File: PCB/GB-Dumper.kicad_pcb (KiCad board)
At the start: 2 copper layers, 89.5 x 72 mm, 27 parts, among them J1 GameBoy_Cartridge_MountingPin, J2 Conn_01x03_Male, J3 Conn_01x02_Male, J4 Conn_01x04_Female, U1 74HC595, U2 74HC595

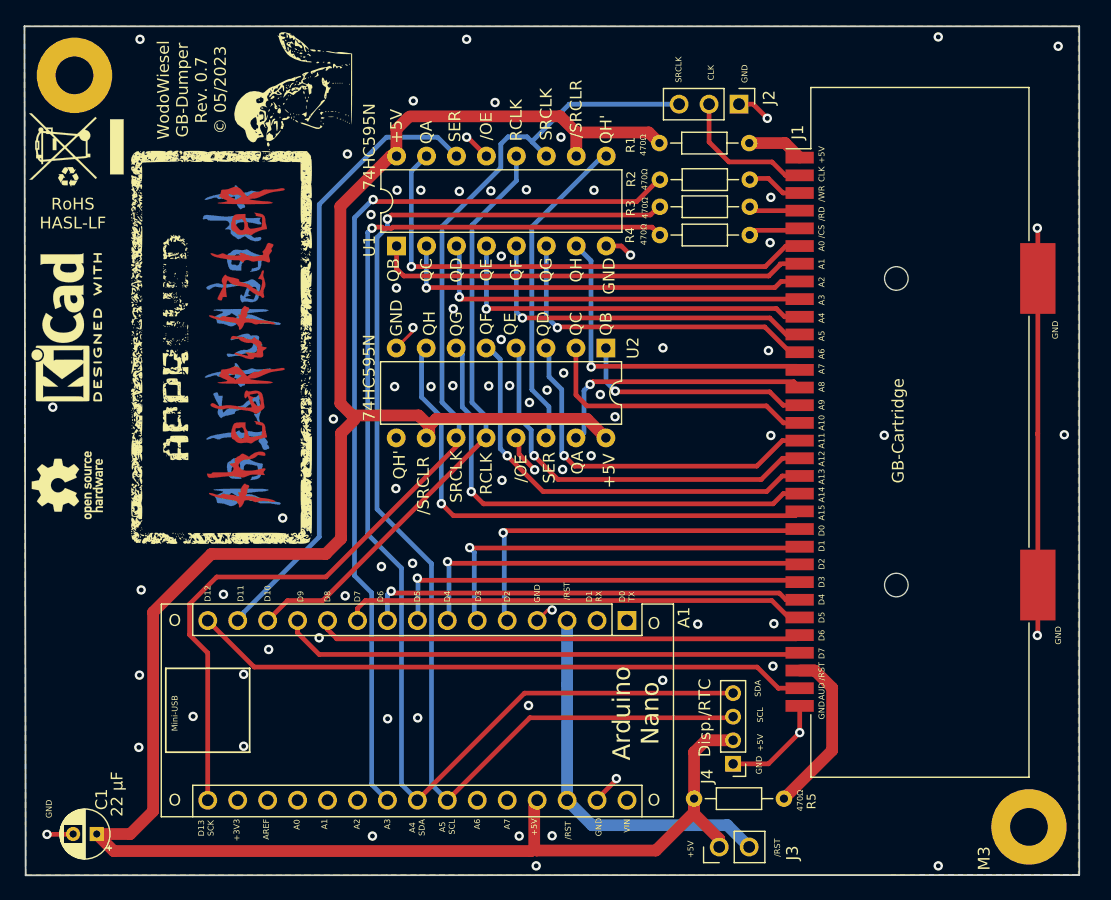
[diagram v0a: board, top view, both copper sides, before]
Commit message: better audio + cs2 + rst button support
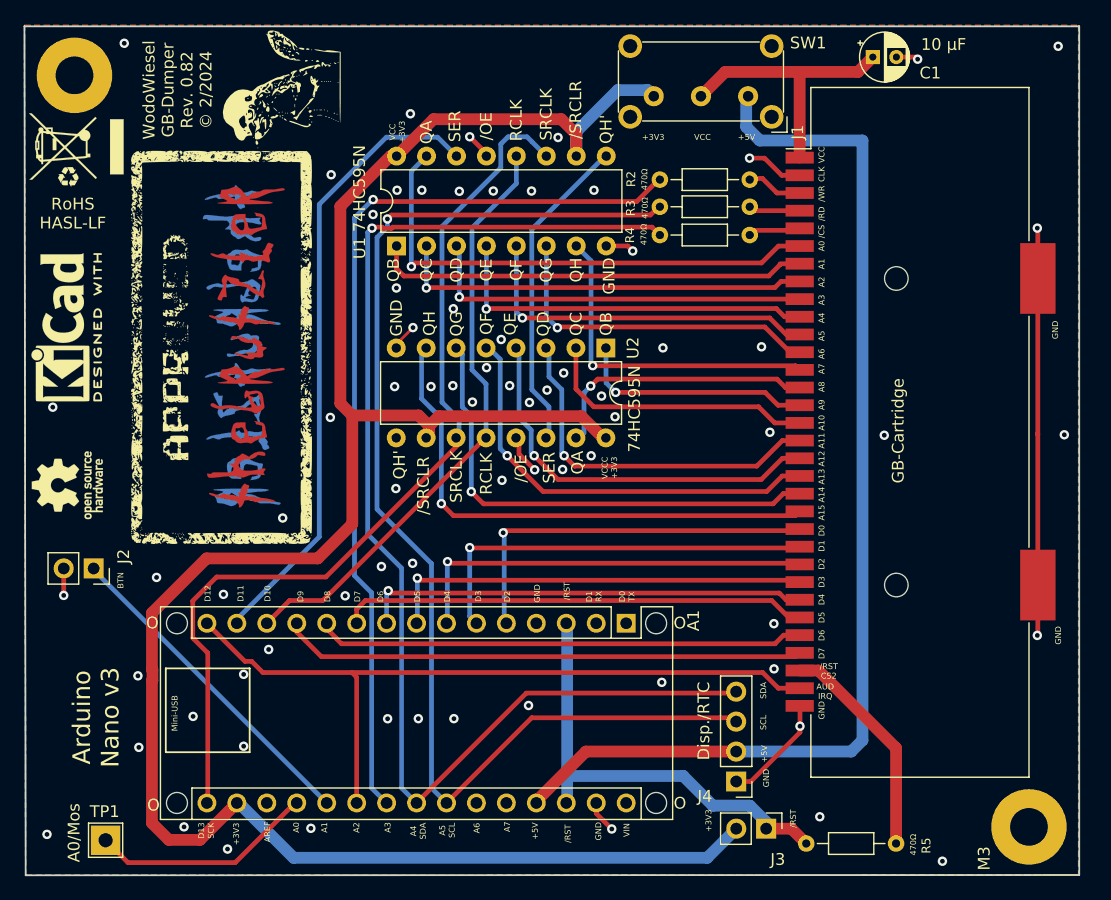
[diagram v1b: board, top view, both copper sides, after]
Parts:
- removed R1: 470Ω, Resistor_THT:R_Axial_DIN0204_L3.6mm_D1.6mm_P7.62mm_Horizontal
- added SW1: SW_DPDT_x2, Button_Switch_THT:SW_E-Switch_EG1224_SPDT_Angled, F.Cu at (245.8, 89.5)
- added TP1: TestPoint, TestPoint:TestPoint_THTPad_2.5x2.5mm_Drill1.2mm, F.Cu at (191.3, 152.6)
- A1: value Arduino_Nano_v3.x -> Arduino_Nano_v3.x_sorted; footprint Module:Arduino_Nano -> Module:Arduino_Nano_WithMountingHoles
- C1: value 22 µF -> 10 µF
- J2: value Conn_01x03_Male -> Conn_01x02_Male; footprint Connector_PinHeader_2.54mm:PinHeader_1x03_P2.54mm_Vertical -> Connector_PinSocket_2.54mm:PinSocket_1x02_P2.54mm_Vertical
- J4: footprint Connector_PinHeader_2.00mm:PinHeader_1x04_P2.00mm_Vertical -> Connector_PinHeader_2.54mm:PinHeader_1x04_P2.54mm_Vertical
- U1, U2: value 74HC595 -> 74HC595_sorted
- moved C1 93.1 mm to (256.3, 86.2), turned to 0 degrees
- moved J2 67.4 mm to (190.2, 129.5)
- moved R5 10.2 mm to (250.7, 152.9)
- moved J3 4.27 mm to (247.3, 151.6), turned to -90 degrees
- moved J4 1.52 mm to (244.7, 147.6)
- moved G2 0.98 mm to (206.2, 88.9)
- moved A1 0.24 mm to (235.4, 134.2)
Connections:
- A1 pad 16: Net-(A1-Pad16) -> Net-(A1-Pad16)_1
- A1 pad 17: unconnected-(A1-Pad17) -> Net-(A1-Pad17)
- A1 pad 19: unconnected-(A1-Pad19) -> Net-(A1-Pad19)
- A1 pad 20: unconnected-(A1-Pad20) -> Net-(A1-Pad20)
- A1 pad 21: unconnected-(A1-Pad21) -> Net-(A1-Pad15)
- A1 pad 29: GND -> Net-(A1-Pad29)
- A1 pad 4: GND -> Net-(A1-Pad29)
- C1 pad 1: Net-(A1-Pad27) -> Net-(C1-Pad1)
- J1 pad 1: Net-(J1-Pad1) -> Net-(C1-Pad1)
- J1 pad 2: Net-(J1-Pad2) -> GND
- J2 pad 1: GND -> Net-(A1-Pad20)
- J2 pad 2: Net-(J1-Pad2) -> GND
- J3 pad 1: Net-(A1-Pad27) -> Net-(A1-Pad28)
- J3 pad 2: Net-(A1-Pad28) -> Net-(A1-Pad17)
- R5 pad 1: Net-(A1-Pad27) -> Net-(A1-Pad28)
- U1 pad 10: Net-(A1-Pad27) -> Net-(A1-Pad17)
- U1 pad 11: Net-(A1-Pad16) -> Net-(A1-Pad16)_1
- U1 pad 13: GND -> Net-(U1-Pad13)
- U1 pad 16: Net-(A1-Pad27) -> Net-(A1-Pad17)
- U1 pad 8: GND -> Net-(U1-Pad13)
- U2 pad 10: Net-(A1-Pad27) -> Net-(A1-Pad17)
- U2 pad 11: Net-(A1-Pad16) -> Net-(A1-Pad16)_1
- U2 pad 16: Net-(A1-Pad27) -> Net-(A1-Pad17)
- U2 pad 8: GND -> Net-(U1-Pad13)
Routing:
- net Net-(A1-Pad17): track 0.00 -> 179.4 mm
- net Net-(A1-Pad27): track 198.0 -> 93.8 mm
- net Net-(A1-Pad16): track 92.5 -> 0.00 mm
- net Net-(A1-Pad16)_1: track 0.00 -> 78.4 mm
- net Net-(A1-Pad20): track 0.00 -> 28.1 mm
- net Net-(C1-Pad1): track 0.00 -> 23.2 mm
- net Net-(A1-Pad19): track 0.00 -> 19.4 mm
- net Net-(J1-Pad2): track 12.1 -> 0.00 mm
- net Net-(A1-Pad15): track 52.6 -> 63.8 mm
- net GND: track 63.8 -> 56.3 mm, vias 78 -> 73
- net Net-(U1-Pad13): track 0.00 -> 6.97 mm
- net Net-(A1-Pad28): track 32.3 -> 38.4 mm
- net Net-(J1-Pad1): track 4.79 -> 0.00 mm
- net Net-(J1-Pad30): track 14.5 -> 19.0 mm
- net Net-(A1-Pad29): track 0.00 -> 2.75 mm
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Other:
- board text added: "/RST CS2"
- board text added: "A0/Mos"
- board text added: "AUD IRQ"
- board text added: "Arduino Nano v3"
- board text added: "BTN"
- board text added: "J2"
- board text added: "J3"
- board text added: "SW1"
- board text added: "TP1"
- board text added: "VCC"
- board text added: "VCC +3V3"
- board text added: "VCCC +3V3"
- board text added: "WodoWiesel GB-Dumper Rev. 0.82 © 2/2024"
- board text removed: "AUD"
- board text removed: "Arduino Nano"
- board text removed: "WodoWiesel GB-Dumper Rev. 0.7 © 05/2023"

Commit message: PCB 0.83 update
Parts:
- removed G2**: LOGO, theBrutzler:thebrutzler_approved_small02
- added BTN: SW_Push, Button_Switch_THT:SW_PUSH_6mm, F.Cu at (187.0, 116.7)
- added G1*: LOGO, the_brutzler_logo:approved_theBrutzler, B.Cu at (196.3, 109.0)
- added J5: Conn_01x03_Pin, Connector_PinHeader_2.54mm:PinHeader_1x03_P2.54mm_Vertical, F.Cu at (230.8, 86.0)
- added J7: Conn_01x06_Pin, Connector_PinHeader_2.54mm:PinHeader_1x06_P2.54mm_Vertical, F.Cu at (191.1, 135.5)
- added R1: 470Ω, Resistor_THT:R_Axial_DIN0204_L3.6mm_D1.6mm_P7.62mm_Horizontal, F.Cu at (246.6, 153.6)
- added REF**: ESD-Logo_6.6x6mm_SilkScreen, Symbol:ESD-Logo_6.6x6mm_SilkScreen, F.Cu at (196.2, 88.3)
- added REF2**: ESD-Logo_6.6x6mm_SilkScreen, Symbol:ESD-Logo_6.6x6mm_SilkScreen, B.Cu at (196.2, 88.3)
- G1: footprint theBrutzler:thebrutzler_approved_small02 -> the_brutzler_logo:approved_theBrutzler
- J2: value Conn_01x02_Male -> Conn_01x03_Pin; footprint Connector_PinSocket_2.54mm:PinSocket_1x02_P2.54mm_Vertical -> Connector_PinHeader_2.54mm:PinHeader_1x03_P2.54mm_Vertical
- J3: value Conn_01x02_Male -> Conn_01x03_Pin; footprint Connector_PinHeader_2.54mm:PinHeader_1x02_P2.54mm_Vertical -> Connector_PinHeader_2.54mm:PinHeader_1x03_P2.54mm_Vertical
- J4: value Conn_01x04_Female -> Conn_01x04_Pin
- SW1: value SW_DPDT_x2 -> SW_SPDT
- moved REF0* 29.1 mm to (196.9, 94.8)
- moved REF0 28.9 mm to (196.9, 94.9)
- moved REF2 24.2 mm to (204.3, 91.2)
- moved REF1* 24.1 mm to (204.3, 91.2)
- moved J3 16.2 mm to (263.4, 149.8)
- moved G2* 15.4 mm to (204.8, 104.1)
- moved G2 15.3 mm to (204.8, 104.1)
- moved J2 11.5 mm to (201.1, 125.6), turned to 90 degrees
- moved J4 7.53 mm to (245.0, 140.1), turned to 0 degrees
- moved G3 5.96 mm to (187.8, 102.3)
- moved G3* 5.96 mm to (188.2, 102.3)
- moved G1 5.16 mm to (196.3, 109.0)
- moved R5 2.79 mm to (248.3, 151.5), turned to 180 degrees
- moved REF4* 1.03 mm to (189.3, 94.8)
- moved REF5 1.03 mm to (189.3, 94.7)
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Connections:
- A1 pad 1: unconnected-(A1-Pad1) -> Net-(A1-D0/PD0/TX)
- A1 pad 15: Net-(A1-Pad15) -> Net-(A1-D12/PB4/MISO)
- A1 pad 17: Net-(A1-Pad17) -> Net-(A1-+3V3)
- A1 pad 2: unconnected-(A1-Pad2) -> Net-(A1-D1/PD1/RX)
- A1 pad 20: Net-(A1-Pad20) -> Net-(A1-A1/PC1)
- A1 pad 21: Net-(A1-Pad15) -> Net-(A1-A2/PC2)
- A1 pad 23: Net-(A1-Pad23) -> Net-(A1-A4/PC4/SDA)
- A1 pad 24: Net-(A1-Pad24) -> Net-(A1-A5/PC5/SCL)
- A1 pad 27: Net-(A1-Pad27) -> Net-(A1-+5V)
- A1 pad 28: Net-(A1-Pad28) -> Net-(J3-Pin_3)
- A1 pad 29: Net-(A1-Pad29) -> GND
- A1 pad 3: Net-(A1-Pad28) -> Net-(J3-Pin_3)
- A1 pad 4: Net-(A1-Pad29) -> GND
- A1 pad 5: Net-(A1-Pad5) -> Net-(A1-D2/PD2/INT0)
- J1 pad 2: GND -> Net-(J1-CLK)
- J1 pad 22: Net-(A1-Pad5) -> Net-(A1-D1/PD1/RX)
- J1 pad 30: Net-(J1-Pad30) -> Net-(J1-~{RES})
- J1 pad 31: Net-(A1-Pad15) -> Net-(J1-VIN)
- J2 pad 1: Net-(A1-Pad20) -> Net-(J1-VIN)
- J2 pad 2: GND -> Net-(A1-D2/PD2/INT0)
- J3 pad 1: Net-(A1-Pad28) -> Net-(A1-D0/PD0/TX)
- J3 pad 2: Net-(A1-Pad17) -> Net-(J1-~{RES})
- J4 pad 1: GND -> Net-(A1-A4/PC4/SDA)
- J4 pad 2: Net-(A1-Pad27) -> Net-(A1-A5/PC5/SCL)
- J4 pad 3: Net-(A1-Pad24) -> Net-(A1-+5V)
- J4 pad 4: Net-(A1-Pad23) -> GND
- R3 pad 1: Net-(A1-Pad24) -> Net-(A1-A5/PC5/SCL)
- R4 pad 1: Net-(A1-Pad23) -> Net-(A1-A4/PC4/SDA)
- R5 pad 1: Net-(A1-Pad28) -> Net-(J1-~{RES})
- R5 pad 2: Net-(J1-Pad30) -> Net-(A1-+3V3)
- SW1 pad 1: Net-(A1-Pad27) -> Net-(A1-+5V)
- SW1 pad 3: Net-(A1-Pad17) -> Net-(A1-+3V3)
- U1 pad 10: Net-(A1-Pad17) -> Net-(A1-+3V3)
- U1 pad 13: Net-(U1-Pad13) -> GND
- U1 pad 16: Net-(A1-Pad17) -> Net-(A1-+3V3)
- U1 pad 8: Net-(U1-Pad13) -> GND
- U2 pad 10: Net-(A1-Pad17) -> Net-(A1-+3V3)
- U2 pad 16: Net-(A1-Pad17) -> Net-(A1-+3V3)
- U2 pad 8: Net-(U1-Pad13) -> GND
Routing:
- net Net-(A1-+3V3): track 0.00 -> 194.8 mm
- net Net-(A1-Pad17): track 179.4 -> 0.00 mm
- net Net-(A1-A4/PC4/SDA): track 0.00 -> 106.8 mm, vias 0 -> 1
- net Net-(A1-Pad23): track 106.5 -> 0.00 mm, vias 1 -> 0
- net Net-(A1-A5/PC5/SCL): track 0.00 -> 104.0 mm, vias 0 -> 1
- net Net-(A1-Pad24): track 103.6 -> 0.00 mm, vias 1 -> 0
- net Net-(A1-Pad27): track 93.8 -> 0.00 mm
- net Net-(A1-+5V): track 0.00 -> 89.1 mm
- net Net-(A1-Pad15): track 63.8 -> 0.00 mm
- net Net-(J1-VIN): track 0.00 -> 59.4 mm, vias 0 -> 1
- net Net-(A1-A1/PC1): track 0.00 -> 55.7 mm, vias 0 -> 2
- net Net-(J3-Pin_3): track 0.00 -> 49.1 mm
- net Net-(A1-D0/PD0/TX): track 0.00 -> 40.2 mm
- net Net-(A1-Pad28): track 38.4 -> 0.00 mm
- net Net-(A1-D2/PD2/INT0): track 0.00 -> 36.1 mm, vias 0 -> 2
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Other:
- board text added: "10 µF"
- board text added: "AUD"
- board text added: "GB31"
- board text added: "GCLK"
- board text added: "IRQ"
- board text added: "J5"
- board text added: "J7"
- board text added: "MISO D12"
- board text added: "MOSI D11"
- board text added: "R1"
- board text added: "R5"
- board text added: "SCK D13"
- board text added: "SCLK"
- board text added: "WodoWiesel GB-Dumper Rev. 0.83 © 6/2024"
- board text added: "~{CS2}"
- board text added: "~{CS}"
- board text added: "~{GB30}"
- board text added: "~{OE}"
- board text added: "~{RD}"
- board text added: "~{RST}"
- board text added: "~{RST} ~{CS2}"
- board text added: "~{SRCLR}"
- board text added: "~{WR}"
- board text removed: "/CS"
- board text removed: "/OE"
- board text removed: "/RD"
- board text removed: "/RST"
- board text removed: "/RST CS2"
- board text removed: "/SRCLR"
- board text removed: "/WR"
- board text removed: "22 µF"
- board text removed: "O"
- board text removed: "WodoWiesel GB-Dumper Rev. 0.82 © 2/2024"

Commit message: -minor optimizations
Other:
- board size 89.5 x 72 mm -> 90.1 x 72 mm
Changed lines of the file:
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@@
 		(tags "THT DIP DIL PDIP 2.54mm 7.62mm 300mil")
 		(property "Reference" "U2"
-			(at -0.01 -2.301 90)
+			(at -2.37 -0.86 90)
 			(layer "F.SilkS")
 			(effects
@@
 		)
 		(property "Value" "74HC595_sorted"
-			(at 5.832 15.733 0)
+			(at 4.05 22.81 90)
 			(layer "F.Fab")
+			(hide yes)
 			(effects
 				(font
@@
 		)
 		(property "Footprint" "Package_DIP:DIP-16_W7.62mm"
-			(at 0 0 -90)
+			(at 2.06 -8.86 -90)
 			(unlocked yes)
 			(layer "F.Fab")
@@
 		)
 		(property "Datasheet" "http://www.ti.com/lit/ds/symlink/sn74hc595.pdf"
-			(at 0 0 -90)
+			(at 1.36 -6.45 -90)
 			(unlocked yes)
 			(layer "F.Fab")
@@
 		)
 		(property "Description" ""
-			(at 0 0 -90)
+			(at 3.64 21.18 -90)
 			(unlocked yes)
 			(layer "F.Fab")
@@
 		)
 		(fp_text user "${REFERENCE}"
-			(at -0.01 -2.301 90)
-			(layer "B.SilkS")
+			(at 3.38 -2.63 90)
+			(layer "B.Fab")
 			(effects
 				(font
@@
 		)
 		(fp_text user "${REFERENCE}"
-			(at -0.022 -2.241 90)
+			(at 3.42 -2.63 90)
 			(layer "F.Fab")
 			(effects
@@
 		)
 		(property "Value" "MountingHole_3.2mm_M3_Pad"
-			(at 0 4.2 0)
+			(at 4.12 5.06 0)
 			(layer "F.Fab")
 			(effects
@@
 	)
 	(gr_line
-		(start 273.834 83.564)
-		(end 273.834 155.54)
+		(start 274.378 83.564)
+		(end 274.479997 155.570438)
 		(stroke
 			(width 0.15)
@@
 	(gr_line
 		(start 184.378 83.564)
-		(end 273.834 83.564)
+		(end 274.378 83.564)
 		(stroke
 			(width 0.15)
@@
 	(gr_line
 		(start 184.478 155.564)
-		(end 184.378 83.564)
+		(end 184.377469 83.56407)
 		(stroke
 			(width 0.15)
@@
 	)
 	(gr_line
-		(start 273.834 155.54)
+		(start 274.479997 155.570438)
 		(end 184.478 155.564)
 		(stroke
@@
 		(layer "Dwgs.User")
 		(pts
-			(xy 184.39 83.56) (xy 273.834 83.564)
+			(xy 184.39 83.56) (xy 274.35 83.57)
 		)
 		(height -3.450234)
-		(gr_text "89.4 mm"
-			(at 229.112205 78.961766 359.9974377)
+		(gr_text "90,0 mm"
+			(at 229.370512 78.964766 359.993631)
 			(layer "Dwgs.User")
 			(effects
@@
 		(layer "Dwgs.User")
 		(pts
-			(xy 184.478 155.564) (xy 184.398 83.584)
+			(xy 184.478 155.564) (xy 184.378 83.564)
 		)
-		(height -6.807473)
-		(gr_text "72.0 mm"
-			(at 178.78053 119.580288 -89.93632036)
+		(height -6.709695)
+		(gr_text "72,0 mm"
+			(at 178.86831 119.571722 -89.92042258)
 			(layer "Dwgs.User")
 			(effects
@@
 		(polygon
 			(pts
-				(xy 273.778 155.564) (xy 184.478 155.564) (xy 184.378 83.474) (xy 273.778 83.474)
+				(xy 274.47 155.58) (xy 184.48 155.57) (xy 184.38 83.57) (xy 274.35 83.57)
 			)
 		)
